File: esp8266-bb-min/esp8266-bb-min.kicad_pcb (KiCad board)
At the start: 2 copper layers, 31.8 x 49.5 mm, 15 parts, among them J1 Conn_01x02_Male, J2 Conn_02x08_Odd_Even, U1 tps77633d-SOIC8, U2 ESP-12F

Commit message: *: cleanup of erc errors
Signed-off-by: Dominik Laton <dominik.laton@web.de>
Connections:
- U1 pad 7: (no net) -> Net-(U1-Pad7)

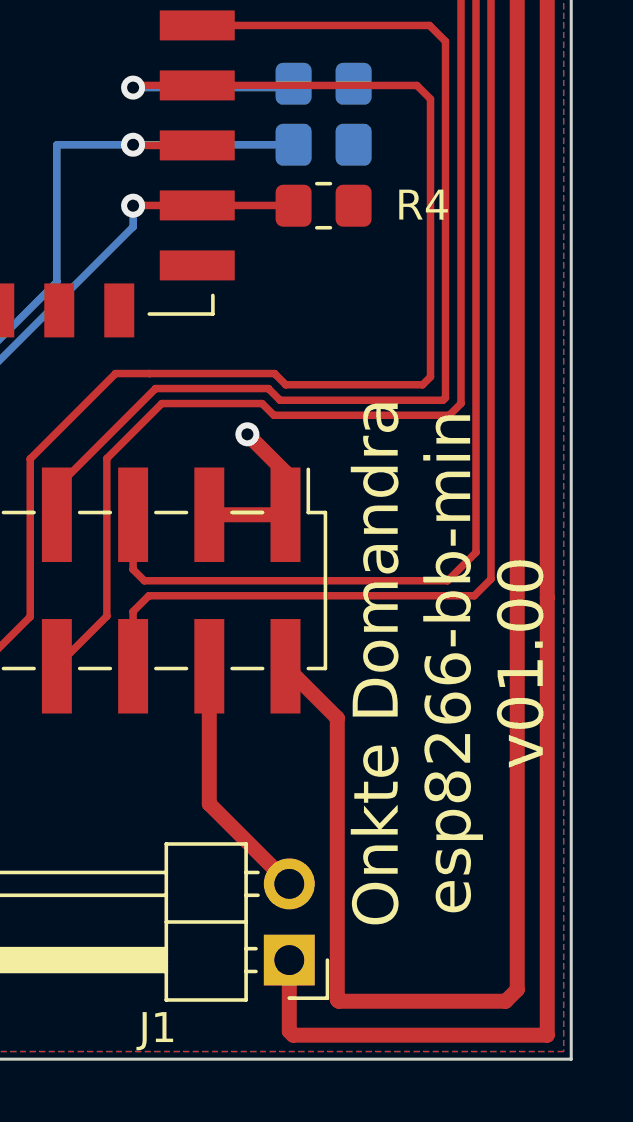
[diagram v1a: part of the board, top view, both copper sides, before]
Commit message: pcb: updated text
Signed-off-by: Dominik Laton <dominik.laton@web.de>
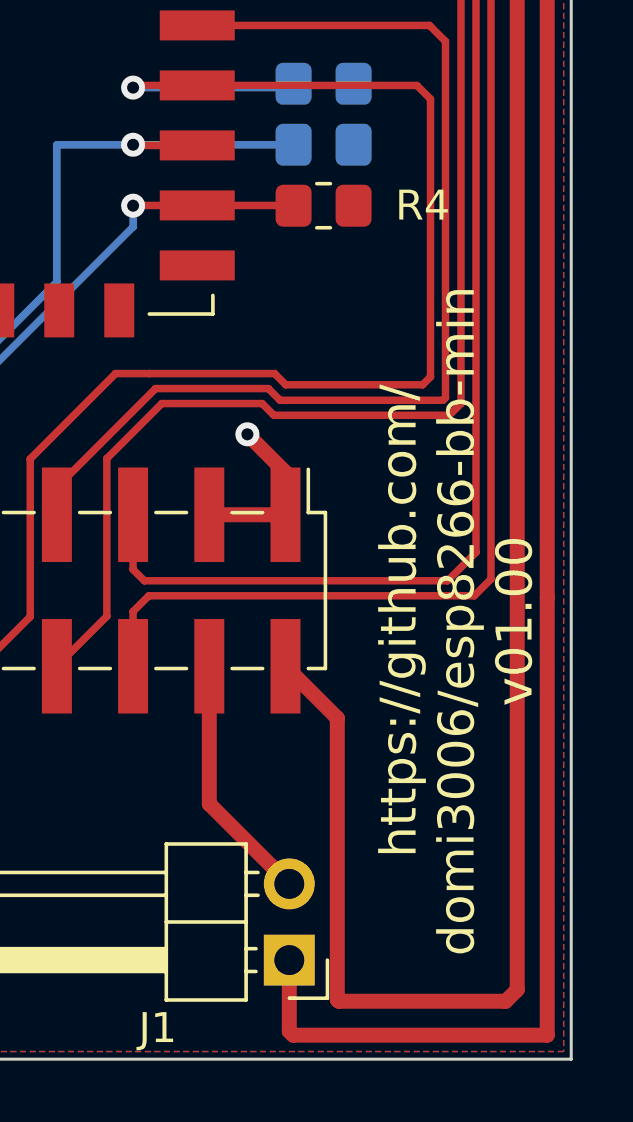
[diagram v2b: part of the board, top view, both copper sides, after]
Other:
- board text added: "https://github.com/ domi3006/esp8266-bb-min v01.00"
- board text removed: "Onkte Domandra esp8266-bb-min v01.00"

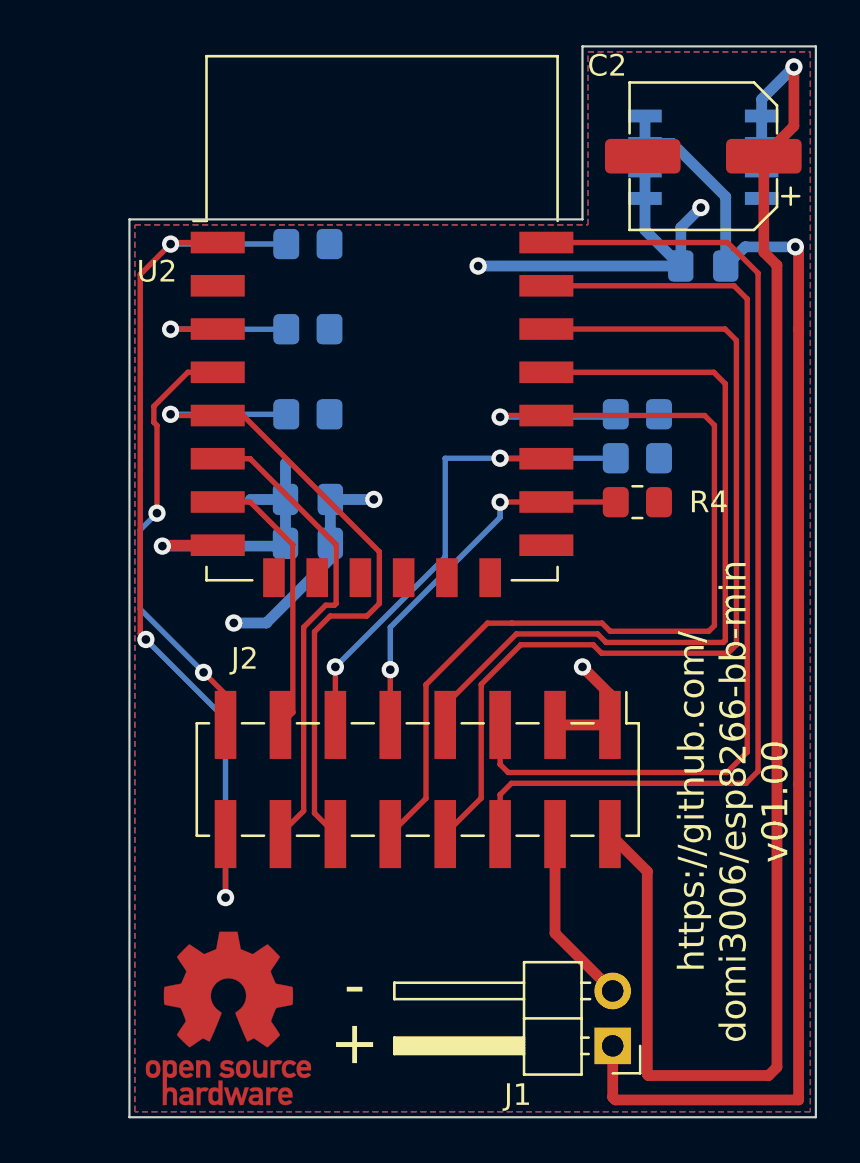
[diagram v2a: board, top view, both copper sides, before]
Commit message: pcb: redesign of pcb
Signed-off-by: Dominik Laton <dominik.laton@web.de>
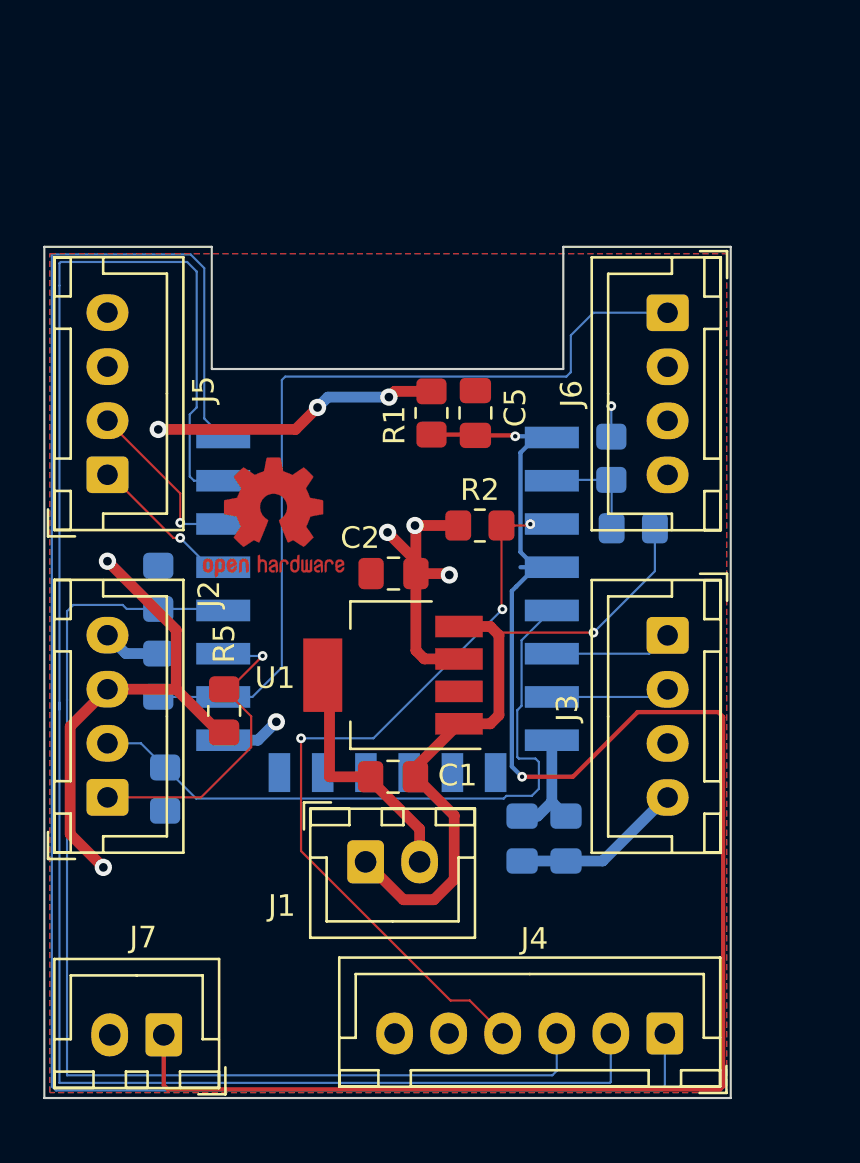
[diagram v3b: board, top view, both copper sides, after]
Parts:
- removed the REF** at (106.2, 107.2)
- added C5: 100nF, Capacitor_SMD:C_0805_2012Metric_Pad1.18x1.45mm_HandSolder, F.Cu at (117.6, 79.2)
- added J3: Conn_01x04_Male, Connector_JST:JST_XH_B4B-XH-A_1x04_P2.50mm_Vertical, F.Cu at (126.5, 89.5)
- added J4: Conn_01x06_Male, Connector_JST:JST_XH_B6B-XH-A_1x06_P2.50mm_Vertical, F.Cu at (126.4, 107.9)
- added J5: Conn_01x04_Male, Connector_JST:JST_XH_B4B-XH-A_1x04_P2.50mm_Vertical, F.Cu at (100.6, 82.0)
- added J6: Conn_01x04_Male, Connector_JST:JST_XH_B4B-XH-A_1x04_P2.50mm_Vertical, F.Cu at (126.5, 74.5)
- added J7: Conn_01x02_Male, Connector_JST:JST_XH_B2B-XH-A_1x02_P2.50mm_Vertical, F.Cu at (103.2, 108.0)
- added R7: 15k, Resistor_SMD:R_0805_2012Metric_Pad1.20x1.40mm_HandSolder, B.Cu at (124.9, 84.5)
- added R8: 39k, Resistor_SMD:R_0805_2012Metric_Pad1.20x1.40mm_HandSolder, B.Cu at (123.9, 81.3)
- added REF**: OSHW-Logo2_7.3x6mm_Copper, Symbol:OSHW-Logo2_7.3x6mm_Copper, F.Cu at (108.3, 84.0)
- C1: value 0.1uF -> 1uF; moved to F.Cu
- C2: value 47uF -> 4.7uF; footprint Capacitor_SMD:CP_Elec_6.3x9.9 -> Capacitor_SMD:C_0805_2012Metric_Pad1.18x1.45mm_HandSolder
- J1: footprint Connector_PinHeader_2.54mm:PinHeader_1x02_P2.54mm_Horizontal -> Connector_JST:JST_XH_B2B-XH-A_1x02_P2.50mm_Vertical
- J2: value Conn_02x08_Odd_Even -> Conn_01x04_Male; footprint Connector_PinHeader_2.54mm:PinHeader_2x08_P2.54mm_Vertical_SMD -> Connector_JST:JST_XH_B4B-XH-A_1x04_P2.50mm_Vertical
- R1, R2, R5: moved to F.Cu
- R4, U2: moved to B.Cu
- U1: value tps77633d-SOIC8 -> LP38693MP-3.3; footprint domi3006:SOIC-8 -> Package_TO_SOT_SMD:SOT-223-5; moved to F.Cu
- moved C1 27.6 mm to (113.8, 96.0)
- moved U1 25.4 mm to (113.8, 91.3), turned to 180 degrees
- moved C2 24.0 mm to (113.8, 86.6)
- moved R4 23.6 mm to (102.9, 91.3), turned to 270 degrees
- moved R3 23.6 mm to (102.9, 87.2), turned to 270 degrees
- moved R5 22.4 mm to (106.0, 93.0), turned to 270 degrees
- moved C3 19.7 mm to (121.8, 98.9), turned to 90 degrees
- moved R6 18.6 mm to (103.3, 96.6), turned to 270 degrees
- moved C4 16.9 mm to (119.8, 98.9), turned to 90 degrees
- moved J2 14.4 mm to (100.6, 97.0), turned to 90 degrees
- moved J1 14.2 mm to (112.5, 99.9), turned to 0 degrees
- moved R2 12.1 mm to (117.8, 84.4), turned to 0 degrees
- moved R1 9.68 mm to (115.6, 79.2), turned to 90 degrees
- moved U2 9.02 mm to (113.5, 83.8), turned to 180 degrees
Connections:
- net Net-(R2-Pad2) renamed /ESP_EN
- C1 pad 2: GND -> -BATT
- C2 pad 1: /3V3_EXT -> +3V3
- C2 pad 2: GND -> -BATT
- C3 pad 1: GND -> -BATT
- C4 pad 1: GND -> -BATT
- J1 pad 2: GND -> -BATT
- J2 pad 1: +3V3 -> /ESP_GPIO2
- J2 pad 2: /3V3_EXT -> /ESP_GPIO14
- J2 pad 4: GND -> -BATT
- R4 pad 1: GND -> -BATT
- U1 pad 1: GND -> +BATT
- U1 pad 2: GND -> Net-(U1-Pad2)
- U1 pad 3: +BATT -> +3V3
- U1 pad 5: /3V3_EXT -> -BATT
- U2 pad 15: GND -> -BATT
- U2 pad 2: Net-(U2-Pad2) -> /ESP_ADC
- U2 pad 4: /ESP_GPIO16 -> /~ESP_RST
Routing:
- net /3V3_EXT: track 69.3 -> 0.00 mm, vias 1 -> 0
- net /~ESP_RST: track 42.9 -> 83.2 mm, vias 3 -> 2
- net /ESP_RXD: track 44.3 -> 83.8 mm
- net /ESP_TXD: track 47.6 -> 85.1 mm
- net GND: track 36.4 -> 0.00 mm, vias 4 -> 0
- net +3V3: track 19.6 -> 55.8 mm, vias 2 -> 8
- net /ESP_GPIO5: track 43.6 -> 8.70 mm, vias 0 -> 1
- net +BATT: track 63.4 -> 32.2 mm
- net /ESP_EN: track 7.53 -> 36.7 mm, vias 1 -> 3
- net /ESP_GPIO4: track 35.8 -> 7.13 mm, vias 0 -> 1
- net -BATT: track 0.00 -> 26.6 mm, vias 0 -> 2
- net /ESP_GPIO15: track 18.7 -> 39.7 mm, vias 2 -> 0
- net /ESP_GPIO16: track 20.4 -> 0.00 mm, vias 2 -> 0
- net /ESP_GPIO12: track 21.8 -> 5.71 mm
- net /ESP_GPIO2: track 24.5 -> 15.5 mm, vias 2 -> 1
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- added copper zone on F.Cu, net -BATT
- removed copper zone on F.Cu, net GND
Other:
- board size 31.8 x 49.5 mm -> 31.8 x 39.4 mm
- net class Default: clearance 0.25 -> 0.2
- net class Max: clearance 0.5 -> 0.3
- rule trace_clearance: 0.25 -> 0.2
- board text added: "3V3"
- board text added: "BATT+"
- board text added: "BATT-"
- board text added: "EN"
- board text added: "GND"
- board text added: "IO0"
- board text added: "IO12"
- board text added: "IO13"
- board text added: "IO14"
- board text added: "IO15"
- board text added: "IO2"
- board text added: "IO4"
- board text added: "IO5"
- board text added: "NC"
- board text added: "RXD"
- board text added: "TXD"
- board text added: "https://github.com/domi3006/esp8266-bb-min v02.00"
- board text added: "~RST"
- board text removed: "+"
- board text removed: "-"
- board text removed: "https://github.com/ domi3006/esp8266-bb-min v01.00"
